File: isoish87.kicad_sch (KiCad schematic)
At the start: 318 parts, among them J1 Conn_01x04_Pin, J3 USB_C_Receptacle_USB2.0_14P, K1 Esc, K10 F9, K11 F10, K12 F11, K13 F12, K14 Print, K15 Scroll, K16 Pause, K17 ` ~, K18 1, K19 2, K2 F1, K20 3, K21 4, K22 5, K23 6, K24 7, K25 8, K26 9, K27 0, K28 - _, K29 = +, K3 F2, K30 Backspace, K31 Ins, K32 Home, K33 PgUp, K34 Tab, K35 Q, K36 W, K37 E, K38 R, K39 T, K4 F3, K40 Y, K41 U, K42 I, K43 O, K44 P, K45 [ {, K46 ] }, K47 Enter, K48 Del, K49 End, K5 F4, K50 PgDn, K51 Caps, K52 A, K53 S, K54 D, K55 F, K56 G, K57 H, K58 J, K59 K, K6 F5, K60 L, K61 ; :, K62 ' ", K63 \ |, K64 LShift, K65 Z, K66 X, K67 C, K68 V, K69 B, K7 F6, K70 N, K71 M, K72 , <, K73 . >, K74 / ?, K75 RShift, K76 Fn, K77 Up, K78 LCtrl, K79 LSys, K8 F7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

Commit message: version 1.1 with proper iso support
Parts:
- removed D1, D10, D11, D12, D13, D14, D15, D16, D17, D18, D19, D2, D20, D21, D22, D23, D24, D25, D26, D27, D28, D29, D3, D30, D31, D32, D33, D34, D35, D36, D37, D38, D39, D4, D40, D41, D42, D43, D44, D45, D46, D47, D48, D49, D5, D50, D51, D52, D53, D54, D55, D56, D57, D58, D59, D6, D60, D61, D62, D63, D64, D65, D66, D67, D68, D69, D7, D70, D71, D72, D73, D74, D75, D76, D77, D78, D79, D8, D80, D81, D82, D83, D84, D85, D86, D87, D9: D, Diode_SMD:D_SOD-323_HandSoldering, symbol Device:D
- added D1, D10, D11, D12, D13, D14, D15, D16, D18, D19, D2, D20, D21, D22, D23, D24, D25, D26, D27, D28, D29, D3, D30, D31, D32, D33, D34, D35, D36, D37, D38, D39, D4, D40, D41, D42, D43, D5, D6, D7, D8, D9: BAV70, schizobovine:SOT-23-1-3-2, symbol Device:D_Dual_CommonCathode_AKA_Split
- added D17, D44, D45, D46: 1N4148W, Diode_SMD:D_SOD-123, symbol Diode:1N4148W
- added JP1: Underglow Bypass, Jumper:SolderJumper-3_P1.3mm_Bridged12_RoundedPad1.0x1.5mm, symbol Jumper:SolderJumper_3_Bridged12
- added K88: NUBS, Switch_Keyboard_Hotswap_Kailh_mine:SW_Hotswap_Kailh_MX_1.00u, symbol keyboard_parts:KEYSW
- added K89: ISOLShift, Switch_Keyboard_Hotswap_Kailh_mine:SW_Hotswap_Kailh_MX_1.25u, symbol keyboard_parts:KEYSW
- added K90: RShift, Switch_Keyboard_Hotswap_Kailh_mine:SW_Hotswap_Kailh_MX_2.75u, symbol keyboard_parts:KEYSW
- added LD88: WS2812B, schizobovine:LED_SK6812MINI_PLCC4_3.1x2.7mm_P1.75mm_reverse_mount, symbol schizobovine:WS2812B
- added SB5: MountingHole, Mounting_Keyboard_Stabilizer:Stabilizer_Cherry_MX_2.00u, symbol Mechanical:MountingHole
- C1, C11, C14, C15, C16, C2, C3, C4, C5, C9: footprint schizobovine:C_0402_1005Metric -> schizobovine:C_0603_1608Metric
- K75: value RShift -> SplitRShift
- R3, R4, R6, R7, R8: footprint schizobovine:R_0402_1005Metric -> schizobovine:R_0603_1608Metric
- R5: value 10K -> 10K DNP; footprint schizobovine:R_0402_1005Metric -> schizobovine:R_0603_1608Metric
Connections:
- net +5V: now also LD88.4 (VDD)
- net GND: now also LD88.2 (VSS)
- net col0: now also K89.2
- net col1: now also K88.1
- net col12: now also K90.2
- net rgb: now also JP1.2 (C); no longer LD1.3 (DIN)
- net row0: now also D1.2 (K), D1.2 (K), D2.2 (K), D2.2 (K), D3.2 (K), D3.2 (K), D4.2 (K), D4.2 (K), D5.2 (K), D5.2 (K), D6.2 (K), D6.2 (K), D7.2 (K), D7.2 (K), D8.2 (K), D8.2 (K)
- net row1: now also D10.2 (K), D10.2 (K), D11.2 (K), D11.2 (K), D12.2 (K), D12.2 (K), D13.2 (K), D13.2 (K), D14.2 (K), D14.2 (K), D15.2 (K), D15.2 (K), D16.2 (K), D16.2 (K), D17.1 (K), D9.2 (K), D9.2 (K)
- net row2: now also D18.2 (K), D18.2 (K), D19.2 (K), D19.2 (K), D20.2 (K), D20.2 (K), D21.2 (K), D21.2 (K), D22.2 (K), D22.2 (K), D23.2 (K), D23.2 (K), D24.2 (K), D24.2 (K), D25.2 (K), D25.2 (K), D44.1 (K)
- net row3: now also D26.2 (K), D26.2 (K), D27.2 (K), D27.2 (K), D28.2 (K), D28.2 (K), D29.2 (K), D29.2 (K), D30.2 (K), D30.2 (K), D31.2 (K), D31.2 (K), D45.1 (K)
- net row4: now also D32.2 (K), D32.2 (K), D33.2 (K), D33.2 (K), D34.2 (K), D34.2 (K), D35.2 (K), D35.2 (K), D36.2 (K), D36.2 (K), D37.2 (K), D37.2 (K), D38.2 (K), D38.2 (K), D46.1 (K)
- net row5: now also D39.2 (K), D39.2 (K), D40.2 (K), D40.2 (K), D41.2 (K), D41.2 (K), D42.2 (K), D42.2 (K), D43.2 (K), D43.2 (K)
- net at K78.2: now also D39.1 (A)
- net at K52.2: now also D26.3 (K)
- net at K53.2: now also D27.1 (A)
- net at K77.2: now also D46.2 (A)
- net at LD75.1 (DOUT): now also LD88.3 (DIN); no longer LD76.3 (DIN)
- net at K5.2: now also D3.1 (A)
- net at K11.2: now also D6.1 (A)
- net at K87.2: now also D43.3 (K)
- net at K42.2: now also D22.1 (A)
- net at K50.2: now also D44.2 (A)
- net at K51.2: now also D26.1 (A)
- net at K10.2: now also D5.3 (K)
- net at K1.2: now also D1.1 (A)
- net at K67.2: now also D34.1 (A)
- net at K39.2: now also D20.3 (K)
- net at K68.2: now also D34.3 (K)
- net at K65.2: now also D33.1 (A)
- net at K31.2: now also D16.1 (A)
- net at K32.2: now also D16.3 (K)
- net at K25.2: now also D13.1 (A)
- net at K34.2: now also D18.1 (A)
- net at K45.2: now also D23.3 (K)
- net at K19.2: now also D10.1 (A)
- net at K38.2: now also D20.1 (A)
- net at K61.2: now also D31.1 (A)
- net at K36.2: now also D19.1 (A)
- net at BD16.3 (DIN), LD78.1 (DOUT): now also JP1.3 (B)
- net at K4.2: now also D2.3 (K)
- net at K46.2: now also D24.1 (A)
- net at K35.2: now also D18.3 (K)
- net at K43.2: now also D22.3 (K)
- net at K13.2: now also D7.1 (A)
- net at K49.2: now also D25.3 (K)
- net at K29.2: now also D15.1 (A)
- net at K30.2: now also D15.3 (K)
- net at K79.2: now also D39.3 (K)
- net at K23.2: now also D12.1 (A)
- net at K60.2: now also D30.3 (K)
- net at K75.2: now also D38.1 (A), K90.1
- net at K17.2: now also D9.1 (A)
- net at K70.2: now also D35.3 (K)
- net at K58.2: now also D29.3 (K)
- net at K40.2: now also D21.1 (A)
- net at K27.2: now also D14.1 (A)
- net at K57.2: now also D29.1 (A)
- net at K73.2: now also D37.1 (A)
- net at K83.2: now also D41.3 (K)
- net at K15.2: now also D8.1 (A)
- net at K63.2: now also D45.2 (A)
- net at K6.2: now also D3.3 (K)
- net at K20.2: now also D10.3 (K)
- net at K47.2: now also D24.3 (K)
- net at K62.2: now also D31.3 (K)
- net at K69.2: now also D35.1 (A)
- net at K81.2: now also D40.3 (K)
- net at K12.2: now also D6.3 (K)
- net at K82.2: now also D41.1 (A)
- net at K37.2: now also D19.3 (K)
- net at K48.2: now also D25.1 (A)
- net at K41.2: now also D21.3 (K)
- net at K44.2: now also D23.1 (A)
- net at K56.2: now also D28.3 (K)
- net at K14.2: now also D7.3 (K)
- net at K80.2: now also D40.1 (A)
- net at K28.2: now also D14.3 (K)
- net at K55.2: now also D28.1 (A)
- net at K22.2: now also D11.3 (K)
- net at K84.2: now also D42.1 (A)
- net at K9.2: now also D5.1 (A)
- net at K76.2: now also D38.3 (K)
- net at K24.2: now also D12.3 (K)
- net at K21.2: now also D11.1 (A)
- net at K64.2: now also D32.1 (A), K89.1
- net at K18.2: now also D9.3 (K)
- net at K2.2: now also D1.3 (K)
- net at K8.2: now also D4.3 (K)
- net at K72.2: now also D36.3 (K)
- net at K7.2: now also D4.1 (A)
- net at K16.2: now also D8.3 (K)
- net at K54.2: now also D27.3 (K)
- net at K59.2: now also D30.1 (A)
- net at K86.2: now also D43.1 (A)
- net at K85.2: now also D42.3 (K)
- net at K66.2: now also D33.3 (K)
- net at K71.2: now also D36.1 (A)
- net at K3.2: now also D2.1 (A)
- net at K74.2: now also D37.3 (K)
- net at K33.2: now also D17.2 (A)
- net at K26.2: now also D13.3 (K)
- new net: JP1.1 (A), LD1.3 (DIN)
- new net: D32.3 (K), K88.2
- new net: LD76.3 (DIN), LD88.1 (DOUT)
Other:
- moved on the sheet: LD1, LD10, LD11, LD12, LD13, LD14, LD15, LD16, LD2, LD3, LD4, LD5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

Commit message: fix spacebar stab alignment, add buffer for RGB
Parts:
- added U1: SN74LVC1G125DBV, Package_TO_SOT_SMD:SOT-23-5, symbol 74xGxx:SN74LVC1G125DBV
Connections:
- net +5V: now also U1.5 (VCC)
- net GND: now also U1.1, U1.3 (GND)
- net gpio: no longer names the net of U5.12 (GPIO9)
- net rgb renamed rgb_3v3
- net rgb_3v3: now also U1.2; no longer JP1.2 (C)
- new net rgb_5v: JP1.2 (C), U1.4
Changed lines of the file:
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@@
   (junction (at 160.782 55.118) (diameter 0) (color 0 0 0 0)
   )
+  (junction (at 440.944 168.91) (diameter 0) (color 0 0 0 0)
+  )
   (junction (at 322.834 55.118) (diameter 0) (color 0 0 0 0)
   )
@@
     (stroke (width 0) (type default))
   )
-  (wire (pts (xy 301.244 159.766) (xy 309.118 159.766))
+  (wire (pts (xy 290.322 160.02) (xy 310.896 160.02))
     (stroke (width 0) (type default))
   )
@@
     (stroke (width 0) (type default))
   )
+  (wire (pts (xy 471.17 168.91) (xy 440.944 168.91))
+    (stroke (width 0) (type default))
+  )
   (wire (pts (xy 221.742 151.13) (xy 221.742 152.4))
     (stroke (width 0) (type default))
@@
     (stroke (width 0) (type default))
   )
-  (wire (pts (xy 309.118 159.766) (xy 309.118 191.262))
+  (wire (pts (xy 310.896 160.02) (xy 310.896 191.008))
     (stroke (width 0) (type default))
   )
@@
     (stroke (width 0) (type default))
   )
-  (wire (pts (xy 540.258 254) (xy 535.94 254))
-    (stroke (width 0) (type default))
-  )
   (wire (pts (xy 178.562 44.958) (xy 178.562 60.198))
     (stroke (width 0) (type default))
@@
     (stroke (width 0) (type default))
   )
-  (wire (pts (xy 301.244 160.02) (xy 301.244 159.766))
-    (stroke (width 0) (type default))
-  )
   (wire (pts (xy 180.848 81.28) (xy 183.642 81.28))
     (stroke (width 0) (type default))
@@
     (stroke (width 0) (type default))
   )
+  (wire (pts (xy 440.944 172.974) (xy 440.944 168.91))
+    (stroke (width 0) (type default))
+  )
   (wire (pts (xy 461.01 271.78) (xy 459.74 271.78))
     (stroke (width 0) (type default))
@@
     (stroke (width 0) (type default))
   )
-  (wire (pts (xy 292.608 191.008) (xy 290.322 191.008))
+  (wire (pts (xy 290.322 191.008) (xy 310.896 191.008))
     (stroke (width 0) (type default))
   )
@@
     (stroke (width 0) (type default))
   )
-  (wire (pts (xy 281.94 139.7) (xy 303.022 139.7))
+  (wire (pts (xy 440.944 168.91) (xy 440.944 165.862))
     (stroke (width 0) (type default))
   )
-  (wire (pts (xy 309.118 191.262) (xy 292.608 191.262))
+  (wire (pts (xy 281.94 139.7) (xy 303.022 139.7))
     (stroke (width 0) (type default))
   )
@@
     (stroke (width 0) (type default))
   )
-  (wire (pts (xy 292.608 191.262) (xy 292.608 191.008))
-    (stroke (width 0) (type default))
-  )
   (wire (pts (xy 58.928 81.28) (xy 61.722 81.28))
     (stroke (width 0) (type default))
@@
     (stroke (width 0) (type default))
   )
-  (wire (pts (xy 290.322 160.02) (xy 301.244 160.02))
-    (stroke (width 0) (type default))
-  )
   (wire (pts (xy 27.178 249.682) (xy 27.178 278.13))
     (stroke (width 0) (type default))
@@
     (stroke (width 0) (type default))
   )
+  (wire (pts (xy 471.17 145.542) (xy 471.17 168.91))
+    (stroke (width 0) (type default))
+  )
   (wire (pts (xy 539.75 220.98) (xy 535.94 220.98))
     (stroke (width 0) (type default))
@@
     (stroke (width 0) (type default))
   )
+  (wire (pts (xy 446.024 145.542) (xy 471.17 145.542))
+    (stroke (width 0) (type default))
+  )
   (wire (pts (xy 180.594 70.358) (xy 201.422 70.358))
     (stroke (width 0) (type default))
@@
     (effects (font (size 1.27 1.27)) (justify left bottom))
   )
-  (global_label "gpio" (shape input) (at 540.258 254 0) (fields_autoplaced)
-    (effects (font (size 1.27 1.27)) (justify left))
-    (property "Intersheetrefs" "${INTERSHEET_REFS}" (at 547.295 254 0)
-      (effects (font (size 1.27 1.27)) (justify left) hide)
-    )
-  )
   (global_label "OUT_USB_D+" (shape input) (at 345.186 312.166 0) (fields_autoplaced)
     (effects (font (size 1.27 1.27)) (justify left))
@@
     )
   )
-  (global_label "rgb" (shape input) (at 28.702 151.13 180) (fields_autoplaced)
+  (global_label "rgb_5v" (shape input) (at 28.702 151.13 180) (fields_autoplaced)
     (effects (font (size 1.27 1.27)) (justify right))
-    (property "Intersheetrefs" "${INTERSHEET_REFS}" (at 22.6326 151.13 0)
+    (property "Intersheetrefs" "${INTERSHEET_REFS}" (at 19.4879 151.13 0)
       (effects (font (size 1.27 1.27)) (justify right) hide)
     )
@@
     )
   )
+  (global_label "rgb_3v3" (shape input) (at 430.784 155.702 180) (fields_autoplaced)
+    (effects (font (size 1.27 1.27)) (justify right))
+    (property "Intersheetrefs" "${INTERSHEET_REFS}" (at 420.3604 155.702 0)
+      (effects (font (size 1.27 1.27)) (justify right) hide)
+    )
+  )
   (global_label "col9" (shape input) (at 237.49 22.86 180)
     (effects (font (size 1.27 1.27)) (justify right))
@@
     )
   )
+  (global_label "rgb_5v" (shape input) (at 458.724 155.702 0) (fields_autoplaced)
+    (effects (font (size 1.27 1.27)) (justify left))
+    (property "Intersheetrefs" "${INTERSHEET_REFS}" (at 467.9381 155.702 0)
+      (effects (font (size 1.27 1.27)) (justify left) hide)
+    )
+  )
   (global_label "col6" (shape input) (at 540.258 281.94 0)
     (effects (font (size 1.27 1.27)) (justify left))
@@
     )
   )
-  (global_label "rgb" (shape input) (at 540.258 251.46 0) (fields_autoplaced)
+  (global_label "rgb_3v3" (shape input) (at 540.258 251.46 0) (fields_autoplaced)
     (effects (font (size 1.27 1.27)) (justify left))
-    (property "Intersheetrefs" "${INTERSHEET_REFS}" (at 546.3274 251.46 0)
+    (property "Intersheetrefs" "${INTERSHEET_REFS}" (at 550.6816 251.46 0)
       (effects (font (size 1.27 1.27)) (justify left) hide)
     )
@@
     )
   )
+  (symbol (lib_id "power:+5V") (at 440.944 145.542 0) (unit 1)
+    (in_bom yes) (on_board yes) (dnp no)
+    (property "Reference" "#PWR021" (at 440.944 149.352 0)
+      (effects (font (size 1.27 1.27)) hide)
+    )
+    (property "Value" "+5V" (at 440.944 141.986 0)
+      (effects (font (size 1.27 1.27)))
+    )
+    (property "Footprint" "" (at 440.944 145.542 0)
+      (effects (font (size 1.27 1.27)) hide)
+    )
+    (property "Datasheet" "" (at 440.944 145.542 0)
+      (effects (font (size 1.27 1.27)) hide)
+    )
+    (pin "1")
+    (instances
+      (project "isoish87"
+        (path "/b531f1c3-24fa-4dc4-abd4-22db5f1ad808"
+          (reference "#PWR021") (unit 1)
+        )
+      )
+    )
+  )
   (symbol (lib_id "keyboard_parts:KEYSW") (at 333.502 44.958 0) (unit 1)
     (in_bom yes) (on_board yes) (dnp no)
@@
     )
   )
+  (symbol (lib_id "74xGxx:SN74LVC1G125DBV") (at 446.024 155.702 0) (unit 1)
+    (in_bom yes) (on_board yes) (dnp no) (fields_autoplaced)
+    (property "Reference" "U1" (at 461.899 151.5111 0)
+      (effects (font (size 1.27 1.27)))
+    )
+    (property "Value" "SN74LVC1G125DBV" (at 461.899 154.0511 0)
+      (effects (font (size 1.27 1.27)))
+    )
+    (property "Footprint" "Package_TO_SOT_SMD:SOT-23-5" (at 446.024 155.702 0)
+      (effects (font (size 1.27 1.27)) hide)
+    )
+    (property "Datasheet" "http://www.ti.com/lit/ds/symlink/sn74lvc1g125.pdf" (at 446.024 155.702 0)
+      (effects (font (size 1.27 1.27)) hide)
+    )
+    (pin "5")
+    (pin "4")
+    (pin "2")
+    (pin "3")
+    (pin "1")
+    (instances
+      (project "isoish87"
+        (path "/b531f1c3-24fa-4dc4-abd4-22db5f1ad808"
+          (reference "U1") (unit 1)
+        )
+      )
+    )
+  )
   (symbol (lib_id "power:GND") (at 220.98 257.302 0) (unit 1)
     (in_bom yes) (on_board yes) (dnp no)
@@
         )
       )
+    )
+  )
+  (symbol (lib_id "power:GND") (at 440.944 172.974 0) (unit 1)
+    (in_bom yes) (on_board yes) (dnp no) (fields_autoplaced)
+    (property "Reference" "#PWR028" (at 440.944 179.324 0)
+      (effects (font (size 1.27 1.27)) hide)
+    )
+    (property "Value" "GND" (at 440.944 178.054 0)
+      (effects (font (size 1.27 1.27)))
+    )
+    (property "Footprint" "" (at 440.944 172.974 0)
+      (effects (font (size 1.27 1.27)) hide)
+    )
+    (property "Datasheet" "" (at 440.944 172.974 0)
+      (effects (font (size 1.27 1.27)) hide)
+    )
+    (pin "1")
+    (instances
+      (project "isoish87"
+        (path "/b531f1c3-24fa-4dc4-abd4-22db5f1ad808"
+          (reference "#PWR028") (unit 1)
+        )
+      )

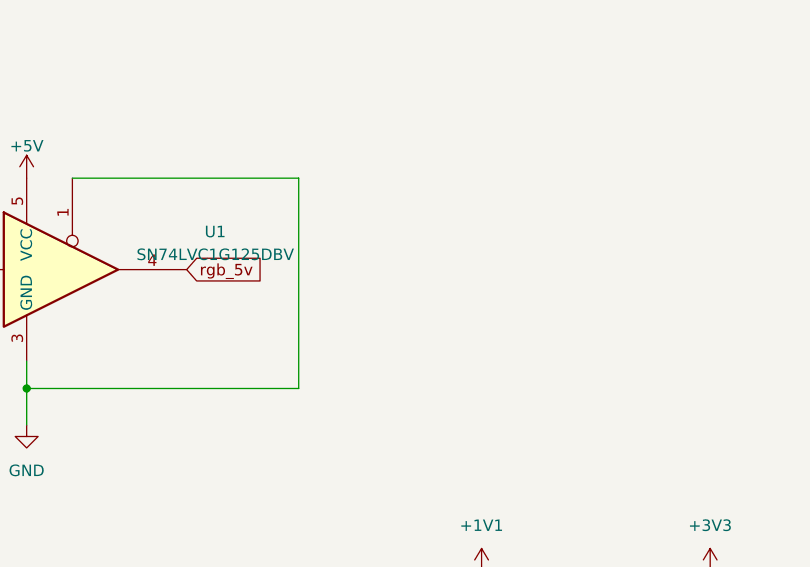
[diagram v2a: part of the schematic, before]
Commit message: add cap for buffer
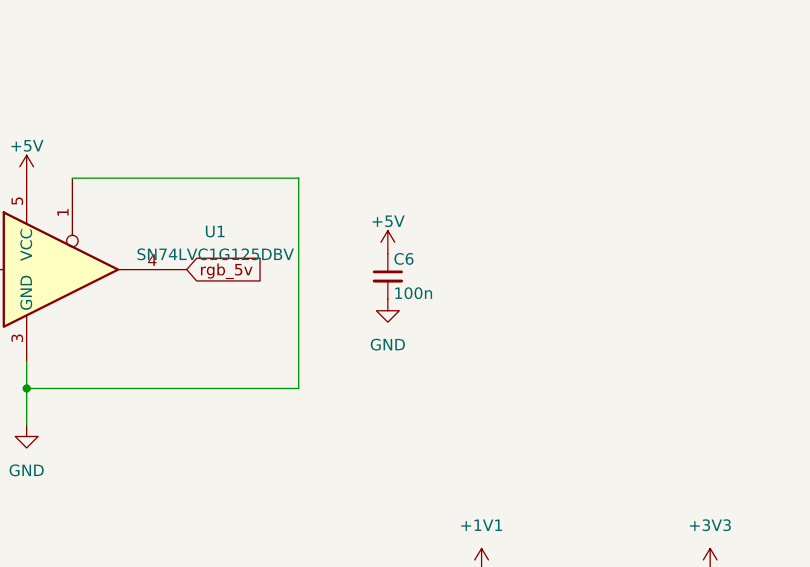
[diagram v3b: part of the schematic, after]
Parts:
- added C6: 100n, schizobovine:C_0603_1608Metric, symbol Device:C_Small
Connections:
- net +5V: now also C6.1
- net GND: now also C6.2
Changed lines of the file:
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@@
     )
   )
+  (symbol (lib_id "power:GND") (at 481.076 159.004 0) (unit 1)
+    (in_bom yes) (on_board yes) (dnp no) (fields_autoplaced)
+    (property "Reference" "#PWR029" (at 481.076 165.354 0)
+      (effects (font (size 1.27 1.27)) hide)
+    )
+    (property "Value" "GND" (at 481.076 164.084 0)
+      (effects (font (size 1.27 1.27)))
+    )
+    (property "Footprint" "" (at 481.076 159.004 0)
+      (effects (font (size 1.27 1.27)) hide)
+    )
+    (property "Datasheet" "" (at 481.076 159.004 0)
+      (effects (font (size 1.27 1.27)) hide)
+    )
+    (pin "1")
+    (instances
+      (project "isoish87"
+        (path "/b531f1c3-24fa-4dc4-abd4-22db5f1ad808"
+          (reference "#PWR029") (unit 1)
+        )
+      )
+    )
+  )
   (symbol (lib_id "schizobovine:WS2812B") (at 191.262 191.008 0) (mirror y) (unit 1)
     (in_bom yes) (on_board yes) (dnp no)
@@
     )
   )
+  (symbol (lib_id "Device:C_Small") (at 481.076 156.464 0) (unit 1)
+    (in_bom yes) (on_board yes) (dnp no)
+    (property "Reference" "C6" (at 481.711 154.559 0)
+      (effects (font (size 1.27 1.27)) (justify left))
+    )
+    (property "Value" "100n" (at 481.711 158.369 0)
+      (effects (font (size 1.27 1.27)) (justify left))
+    )
+    (property "Footprint" "schizobovine:C_0603_1608Metric" (at 481.076 156.464 0)
+      (effects (font (size 1.27 1.27)) hide)
+    )
+    (property "Datasheet" "~" (at 481.076 156.464 0)
+      (effects (font (size 1.27 1.27)) hide)
+    )
+    (pin "1")
+    (pin "2")
+    (instances
+      (project "isoish87"
+        (path "/b531f1c3-24fa-4dc4-abd4-22db5f1ad808"
+          (reference "C6") (unit 1)
+        )
+      )
+    )
+  )
   (symbol (lib_id "power:+5V") (at 282.194 213.614 0) (unit 1)
     (in_bom yes) (on_board yes) (dnp no)
@@
         )
       )
+    )
+  )
+  (symbol (lib_id "power:+5V") (at 481.076 153.924 0) (unit 1)
+    (in_bom yes) (on_board yes) (dnp no)
+    (property "Reference" "#PWR030" (at 481.076 157.734 0)
+      (effects (font (size 1.27 1.27)) hide)
+    )
+    (property "Value" "+5V" (at 481.076 150.368 0)
+      (effects (font (size 1.27 1.27)))
+    )
+    (property "Footprint" "" (at 481.076 153.924 0)
+      (effects (font (size 1.27 1.27)) hide)
+    )
+    (property "Datasheet" "" (at 481.076 153.924 0)
+      (effects (font (size 1.27 1.27)) hide)
+    )
+    (pin "1")
+    (instances
+      (project "isoish87"
+        (path "/b531f1c3-24fa-4dc4-abd4-22db5f1ad808"
+          (reference "#PWR030") (unit 1)
+        )
+      )
